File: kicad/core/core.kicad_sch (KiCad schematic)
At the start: 100 parts, among them J1 X_HS0_n, J10 ADDR_A0, J11 ADDR_A1, J12 ADDR_A2, J13 DEC_EN, J14 FWD_EN_n, J15 REV_EN_n, J2 Y_HS0_n, J3 X_LS0_n, J4 Y_LS0_n, J5 INH_EN_n, J6 X_HS0r_n, J7 Y_HS0r_n, J8 X_LS0r_n, J9 Y_LS0r_n, Q1 IRLZ44N, Q2 FDS8958A, Q3 FDS8958A, Q4 FDS8958A, Q5 FDS8958A, Q6 FDS8958A, U1 TLV3501AID, U10 TC4426A, U11 74AHC138, U12 74AHC138, U13 74AHC138, U14 74AHC138, U15 74AHC125, U16 74AHC125, U2 74AHC74, U3 OPA192, U4 TL431LP, U5 TC4427A, U6 TC4426A, U7 TC4427A, U8 TC4426A, U9 TC4427A

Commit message: logical schematic blocks reorg
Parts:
- removed U15, U16: 74AHC125, Package_SO:SOIC-14_3.9x8.7mm_P1.27mm, symbol 74xx:74LS125
- added C25, C26: 100n, Capacitor_SMD:C_0805_2012Metric, symbol Device:C
- added U15, U16, U17, U18: 74AHC138, Package_SO:SOIC-16_3.9x9.9mm_P1.27mm, symbol 74xx:74HC138
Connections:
- net DEC_XH0 is gone; now on net X_HS0_n: U11.15 (~{Y0})
- net DEC_XL0 is gone; now on net X_LS0_n: U12.15 (~{Y0})
- net DEC_YH0 is gone; now on net Y_HS0_n: U13.15 (~{Y0})
- net DEC_YL0 is gone; now on net Y_LS0_n: U14.15 (~{Y0})
- net +3V3: now also C25.1, C25.2, C26.1, C26.2, U15.16 (VCC), U15.5 (~{E1}), U15.8 (GND), U16.16 (VCC), U16.5 (~{E1}), U16.8 (GND), U17.16 (VCC), U17.5 (~{E1}), U17.8 (GND), U18.16 (VCC), U18.5 (~{E1}), U18.8 (GND); no longer J13.1 (Pin_1), R22.1, U11.4 (~{E0}), U11.6 (E2), U12.4 (~{E0}), U12.6 (E2), U13.4 (~{E0}), U13.6 (E2), U14.4 (~{E0}), U14.6 (E2)
- net ADDR_A0: now also U15.1 (A0), U16.1 (A0), U17.1 (A0), U18.1 (A0)
- net ADDR_A1: now also U15.2 (A1), U16.2 (A1), U17.2 (A1), U18.2 (A1)
- net ADDR_A2: now also U15.3 (A2), U16.3 (A2), U17.3 (A2), U18.3 (A2)
- net FWD_EN_n: now also U11.4 (~{E0}), U12.4 (~{E0}), U13.4 (~{E0}), U14.4 (~{E0})
- net REV_EN_n: now also U15.4 (~{E0}), U16.4 (~{E0}), U17.4 (~{E0}), U18.4 (~{E0})
- net X_HS0r_n: now also U15.15 (~{Y0})
- net X_LS0r_n: now also U16.15 (~{Y0})
- net Y_HS0r_n: now also U17.15 (~{Y0})
- net Y_LS0r_n: now also U18.15 (~{Y0})
- new net DEC_EN: J13.1 (Pin_1), R22.1, U11.6 (E2), U12.6 (E2), U13.6 (E2), U14.6 (E2), U15.6 (E2), U16.6 (E2), U17.6 (E2), U18.6 (E2)
- no-connect marks 52 -> 80
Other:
- note added: "CCS — Ic/2 sink"
- note added: "DECODE — FWD/REV 138 banks (1×1 / Y0)"
- note added: "DECODE: 74AHC138×4 FWD + ×4 REV; ~E0←FWD/REV_EN_n, ~E1←GND, E2←DEC_EN; ~Y0→*_n/*r_n; never assert both EN"
- note added: "DRIVE FWD — X0/Y0 matrix + gate"
- note added: "DRIVE REV — X0/Y0 matrix + gate"
- note added: "INHIBIT — series YB65→fold→YB66→CCS"
- note added: "QX/QY FDS8958A + SS14 → XA0/XB0 & YA0/YB0; LS → CCS_RET; TC442x below"
- note added: "QX0r/QY0r FDS8958A + SS14 swapped ends (HS→XB0/YB0, LS←XA0/YA0); LS→CCS_RET; TC442x below"
- note added: "SENSE — Bowtie / latch"
- note added: "SENSE — Bowtie / split-sense + amp Clamps: BAT54S rot90 — +3V3 (K) above, GND (A) below C1/C2 at U1; C3/C4 at U2; blocks spaced for hand placement"
- note added: "TL431 2.5V + pot divider → VSET; OPA192 drives IRLZ44N via R8; R9=1Ω; CCS_RET → Drive FWD/REV + Inhibit"
- note removed: "74AHC138×4 → DEC_*0; 74AHC125×2 steer FWD_EN_n→*_n / REV_EN_n→*r_n; ADDR default 000; never assert both EN"
- note removed: "QX/QY FDS8958A + SS14 → XA0/XB0 & YA0/YB0; LS → CCS_RET; gates labeled for Stage 4"
- note removed: "QX0r/QY0r FDS8958A + SS14 swapped ends (HS→XB0/YB0, LS←XA0/YA0); LS→CCS_RET; gates for Stage 7"
- note removed: "STAGE 1 — Sense / Bowtie"
- note removed: "STAGE 2 — CCS (Ic/2 sink)"
- note removed: "STAGE 3 — X/Y forward drive"
- note removed: "STAGE 4 — Gate drive (fail-safe pull-ups)"
- note removed: "STAGE 5 — Inhibit (series YB65→bowtie→YB66→CCS)"
- note removed: "STAGE 6 — X/Y reverse WRITE drive"
- note removed: "STAGE 7 — Reverse gate drive (fail-safe pull-ups)"
- note removed: "STAGE 8 — Address decode (1×1 / Y0 only)"
- note removed: "Stage 1 — Bowtie / split-sense + amp Clamps: BAT54S rot90 — +3V3 (K) above, GND (A) below C1/C2 at U1; C3/C4 at U2; blocks spaced for hand placement"
- note removed: "TL431 2.5V + pot divider → VSET; OPA192 drives IRLZ44N via R8; R9=1Ω; CCS_RET → Stage 3/5"
- title: Core Memory Driver — Stage 1 Sense / Bowtie -> Core Memory Driver

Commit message: Split the schematic into hierarchical blocks and document the net grammar.
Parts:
- removed C1, C11, C13, C15, C17, C19, C20, C21, C22, C23, C24, C25, C26, C3, C5, C7, C9: 100n, Capacitor_SMD:C_0805_2012Metric, symbol Device:C
- removed C10, C12, C14, C16, C18, C2, C4, C6, C8: 1u, Capacitor_SMD:C_0805_2012Metric, symbol Device:C
- removed D1, D2: BAT54S, Package_TO_SOT_SMD:SOT-23, symbol Diode:BAT54S
- removed D10, D3, D4, D5, D6, D7, D8, D9: SS14, Diode_SMD:D_SMA, symbol Diode:SS14
- removed FB1: FB_A, Inductor_SMD:L_1206_3216Metric, symbol core_memory:CoreBead_3W
- removed FB2: FB_B, Inductor_SMD:L_1206_3216Metric, symbol core_memory:CoreBead_3W
- removed J1: X_HS0_n, Connector_PinHeader_2.54mm:PinHeader_1x01_P2.54mm_Vertical, symbol Connector:Conn_01x01
- removed J10: ADDR_A0, Connector_PinHeader_2.54mm:PinHeader_1x01_P2.54mm_Vertical, symbol Connector:Conn_01x01
- removed J11: ADDR_A1, Connector_PinHeader_2.54mm:PinHeader_1x01_P2.54mm_Vertical, symbol Connector:Conn_01x01
- removed J12: ADDR_A2, Connector_PinHeader_2.54mm:PinHeader_1x01_P2.54mm_Vertical, symbol Connector:Conn_01x01
- removed J13: DEC_EN, Connector_PinHeader_2.54mm:PinHeader_1x01_P2.54mm_Vertical, symbol Connector:Conn_01x01
- removed J14: FWD_EN_n, Connector_PinHeader_2.54mm:PinHeader_1x01_P2.54mm_Vertical, symbol Connector:Conn_01x01
- removed J15: REV_EN_n, Connector_PinHeader_2.54mm:PinHeader_1x01_P2.54mm_Vertical, symbol Connector:Conn_01x01
- removed J2: Y_HS0_n, Connector_PinHeader_2.54mm:PinHeader_1x01_P2.54mm_Vertical, symbol Connector:Conn_01x01
- removed J3: X_LS0_n, Connector_PinHeader_2.54mm:PinHeader_1x01_P2.54mm_Vertical, symbol Connector:Conn_01x01
- removed J4: Y_LS0_n, Connector_PinHeader_2.54mm:PinHeader_1x01_P2.54mm_Vertical, symbol Connector:Conn_01x01
- removed J5: INH_EN_n, Connector_PinHeader_2.54mm:PinHeader_1x01_P2.54mm_Vertical, symbol Connector:Conn_01x01
- removed J6: X_HS0r_n, Connector_PinHeader_2.54mm:PinHeader_1x01_P2.54mm_Vertical, symbol Connector:Conn_01x01
- removed J7: Y_HS0r_n, Connector_PinHeader_2.54mm:PinHeader_1x01_P2.54mm_Vertical, symbol Connector:Conn_01x01
- removed J8: X_LS0r_n, Connector_PinHeader_2.54mm:PinHeader_1x01_P2.54mm_Vertical, symbol Connector:Conn_01x01
- removed J9: Y_LS0r_n, Connector_PinHeader_2.54mm:PinHeader_1x01_P2.54mm_Vertical, symbol Connector:Conn_01x01
- removed Q1: IRLZ44N, Package_TO_SOT_THT:TO-220-3_Vertical, symbol Transistor_FET:IRLZ44N
- removed Q2, Q3, Q4, Q5, Q6: FDS8958A, Package_SO:SOIC-8_3.9x4.9mm_P1.27mm, symbol core_memory:FDS8958A
- removed R1, R10, R11, R12, R13, R14, R15, R16, R17, R18, R19, R20, R21, R22, R23, R24, R6: 10k, Resistor_SMD:R_0805_2012Metric, symbol Device:R
- removed R2, R5: DNP, Resistor_SMD:R_0805_2012Metric, symbol Device:R
- removed R3, R4, R7: 1k, Resistor_SMD:R_0805_2012Metric, symbol Device:R
- removed R8: 100, Resistor_SMD:R_0805_2012Metric, symbol Device:R
- removed R9: 1, Resistor_SMD:R_2512_6332Metric, symbol Device:R
- removed RV1: 10k, Potentiometer_THT:Potentiometer_Bourns_3296W_Vertical, symbol Device:R_Potentiometer_US
- removed TP1: DOUT, TestPoint:TestPoint_Pad_D1.5mm, symbol Connector:TestPoint
- removed TP2: Isense, TestPoint:TestPoint_Pad_D1.5mm, symbol Connector:TestPoint
- removed U1: TLV3501AID, Package_SO:SOIC-8_3.9x4.9mm_P1.27mm, symbol Comparator:TLV3501AID
- removed U10, U6, U8: TC4426A, Package_SO:SOIC-8_3.9x4.9mm_P1.27mm, symbol Driver_FET:TC4426xOA
- removed U11, U12, U13, U14, U15, U16, U17, U18: 74AHC138, Package_SO:SOIC-16_3.9x9.9mm_P1.27mm, symbol 74xx:74HC138
- removed U2: 74AHC74, Package_SO:SOIC-14_3.9x8.7mm_P1.27mm, symbol 74xx:74LS74
- removed U3: OPA192, Package_SO:SOIC-8_3.9x4.9mm_P1.27mm, symbol core_memory:OPA192
- removed U4: TL431LP, Package_TO_SOT_THT:TO-92_Inline, symbol Reference_Voltage:TL431LP
- removed U5, U7, U9: TC4427A, Package_SO:SOIC-8_3.9x4.9mm_P1.27mm, symbol Driver_FET:TC4427xOA
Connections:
- no-connect marks 80 -> 8
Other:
- added sheet CCS (ccs.kicad_sch)
- added sheet Decode Block (decode_block.kicad_sch)
- added sheet Decode CTRL (decode_ctrl.kicad_sch)
- added sheet Decoupling Logic (decoupling_logic.kicad_sch)
- added sheet Decoupling VDRIVE (decoupling_vdrive.kicad_sch)
- added sheet Drive Block (drive_block.kicad_sch)
- added sheet Ferrite Beads (ferrite_beads.kicad_sch)
- added sheet Inhibit (inhibit.kicad_sch)
- added sheet Sense (sense.kicad_sch)
- note added: "DECODE — Decode Block (N=axis, n=HS/LS bank); X FWD wired for 1×1 bring-up"
- note added: "DRIVE — Drive Block (N=axis, n=line); X0 FWD wired for 1×1 bring-up"
- note added: "Decoupling (global power) — caps off the signal pages"
- note added: "SENSE / FERRITE BEADS / CCS / INHIBIT / DECODE CTRL — hierarchy"
- note removed: "CCS — Ic/2 sink"
- note removed: "DECODE — FWD/REV 138 banks (1×1 / Y0)"
- note removed: "DECODE: 74AHC138×4 FWD + ×4 REV; ~E0←FWD/REV_EN_n, ~E1←GND, E2←DEC_EN; ~Y0→*_n/*r_n; never assert both EN"
- note removed: "DRIVE FWD — X0/Y0 matrix + gate"
- note removed: "DRIVE REV — X0/Y0 matrix + gate"
- note removed: "INHIBIT — series YB65→fold→YB66→CCS"
- note removed: "QX/QY FDS8958A + SS14 → XA0/XB0 & YA0/YB0; LS → CCS_RET; TC442x below"
- note removed: "QX0r/QY0r FDS8958A + SS14 swapped ends (HS→XB0/YB0, LS←XA0/YA0); LS→CCS_RET; TC442x below"
- note removed: "SENSE — Bowtie / latch"
- note removed: "SENSE — Bowtie / split-sense + amp Clamps: BAT54S rot90 — +3V3 (K) above, GND (A) below C1/C2 at U1; C3/C4 at U2; blocks spaced for hand placement"
- note removed: "TC4427A → X/Y_HS0; TC4426A → X/Y_LS0; 10k to +3V3 on *_n; VDRIVE power; headers J1–J4"
- note removed: "TC4427A → X/Y_HS0r; TC4426A → X/Y_LS0r; 10k to +3V3 on *r_n; headers J6–J9"
- note removed: "TL431 2.5V + pot divider → VSET; OPA192 drives IRLZ44N via R8; R9=1Ω; CCS_RET → Drive FWD/REV + Inhibit"

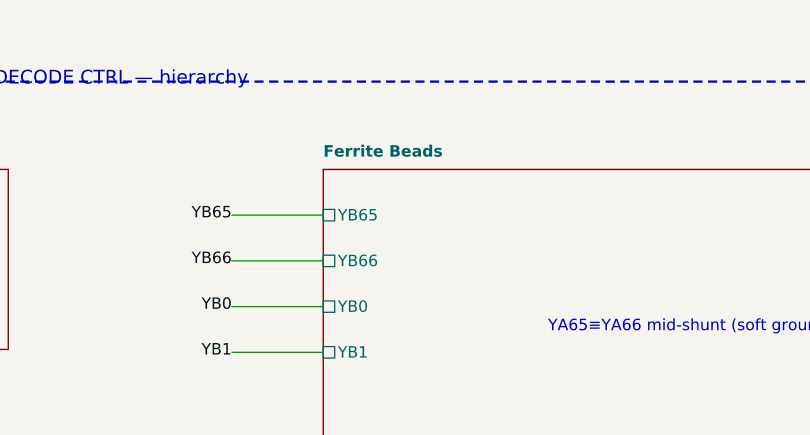
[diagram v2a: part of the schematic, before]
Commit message: created new component based on simulation and replace resistive model with inductive model
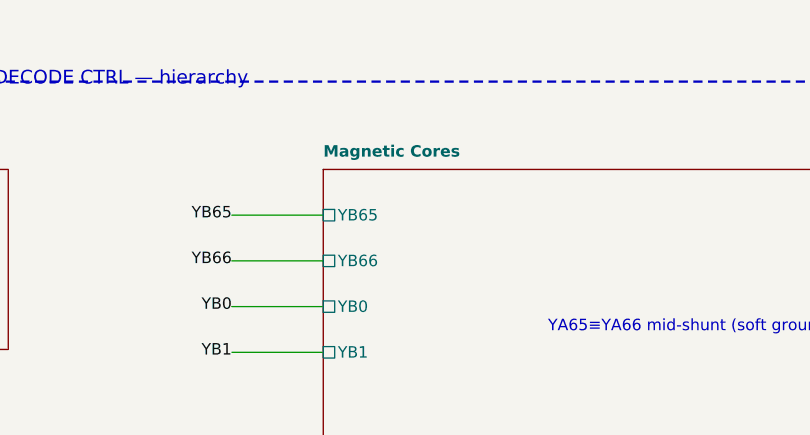
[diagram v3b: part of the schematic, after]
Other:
- sheet Ferrite Beads renamed Magnetic Cores
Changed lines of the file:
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@@
 			(color 0 0 0 0)
 		)
-		(property "Sheetname" "Ferrite Beads"
+		(property "Sheetname" "Magnetic Cores"
 			(at 100 23.73 0)
 			(show_name no)

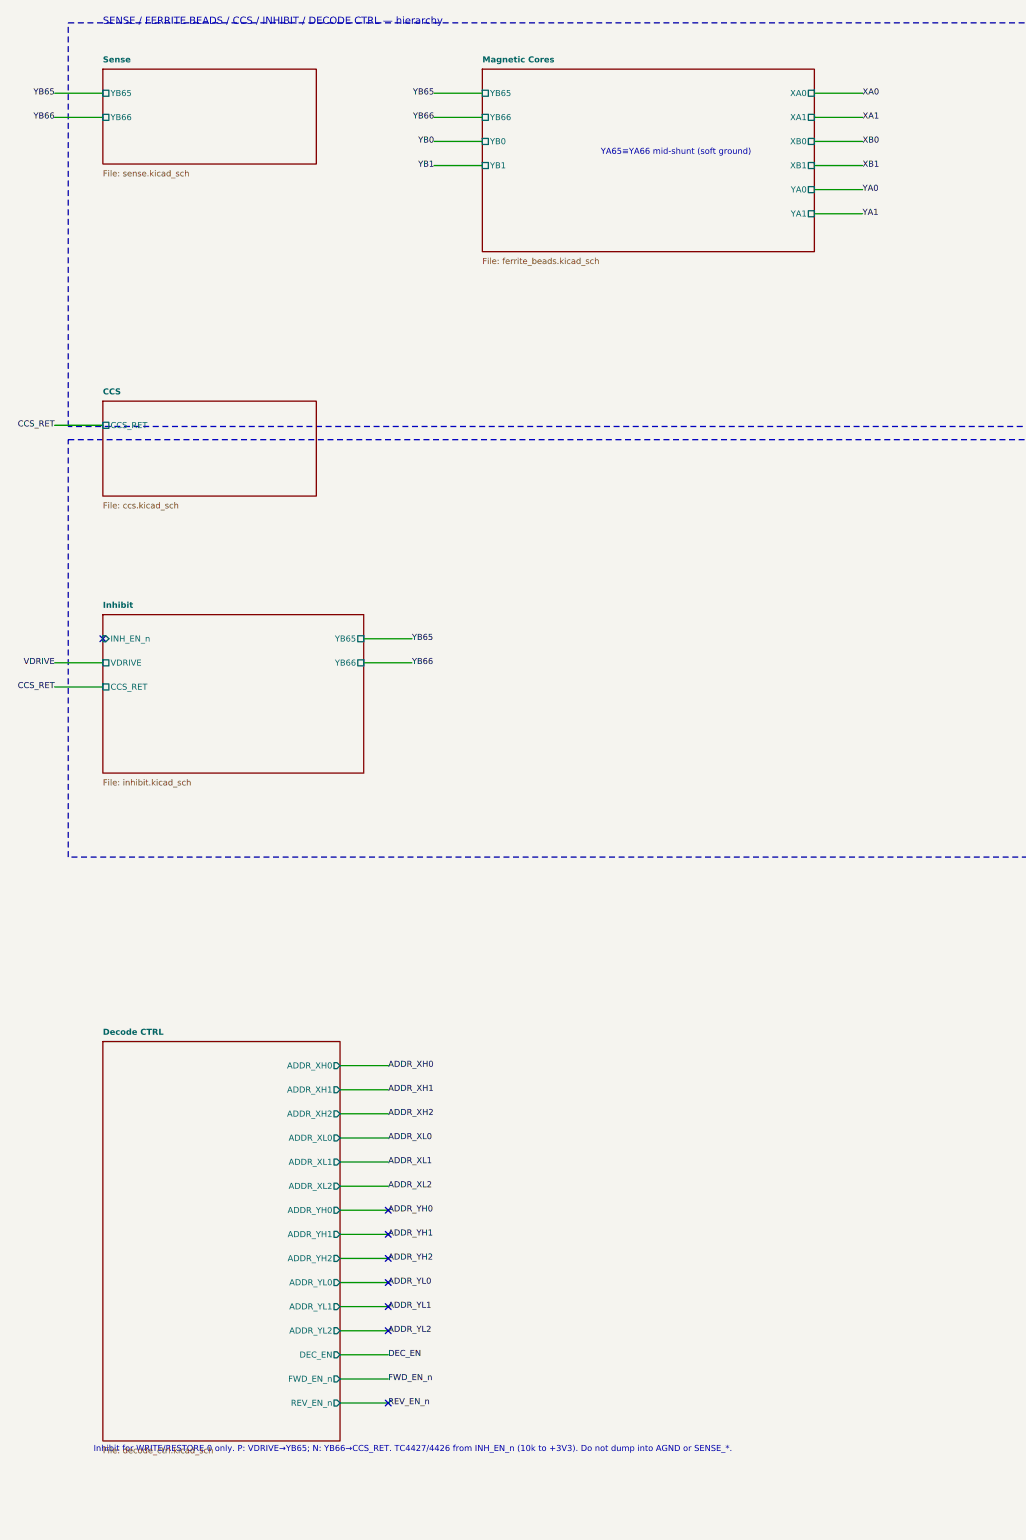
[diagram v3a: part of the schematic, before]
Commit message: Docs updated to match physical core layout.
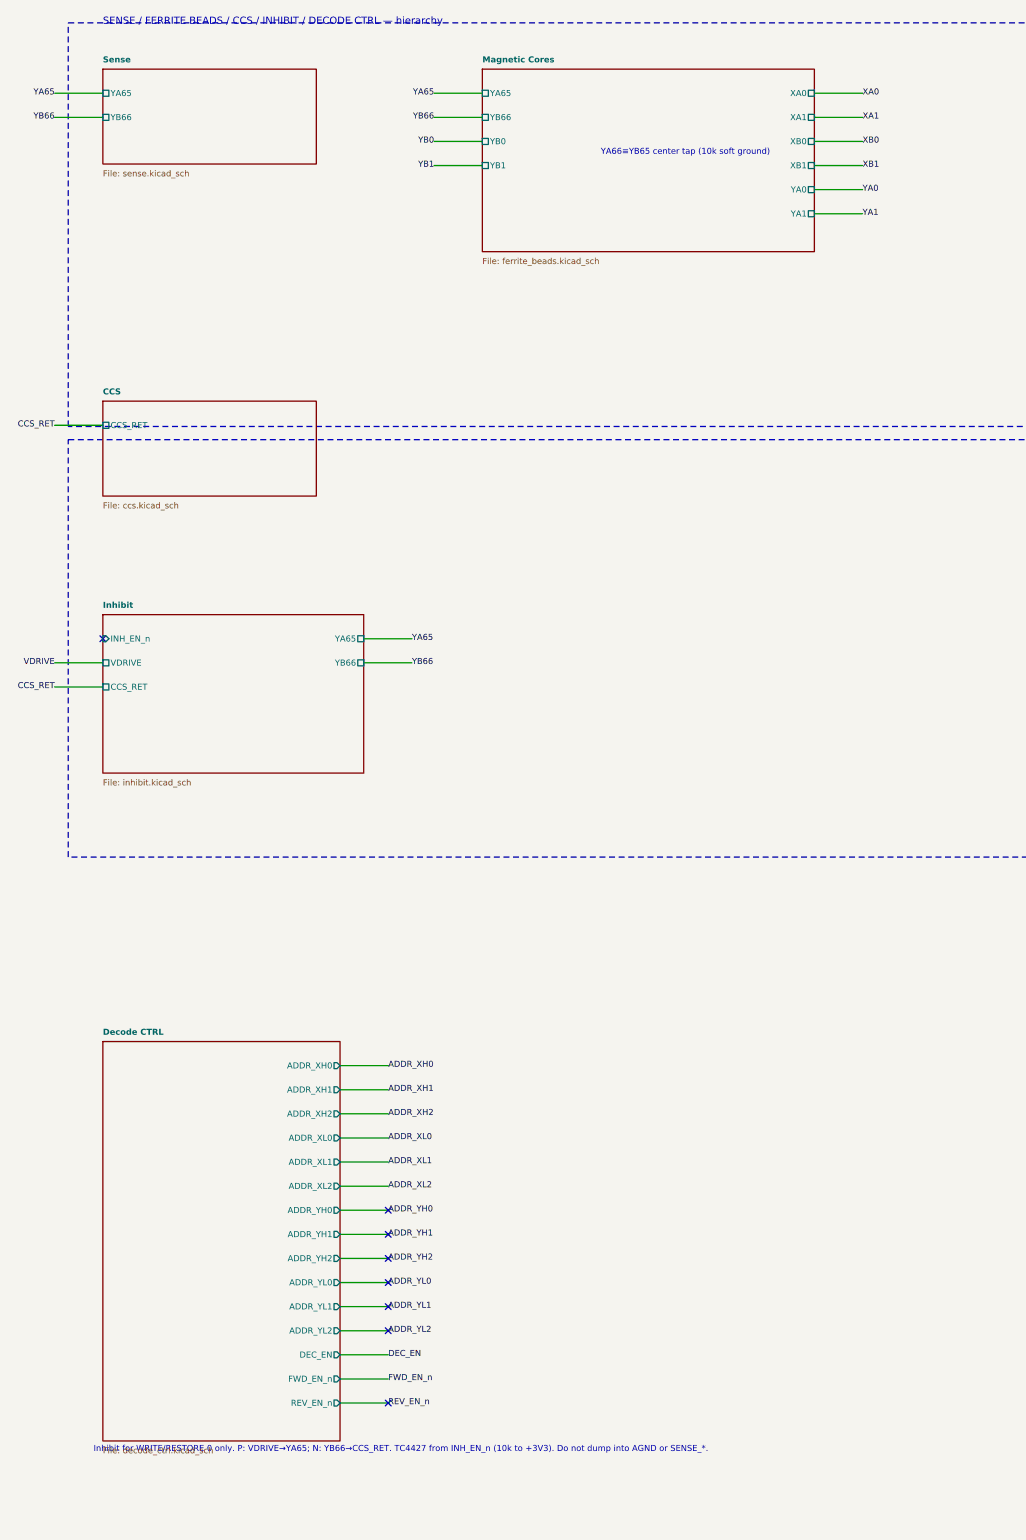
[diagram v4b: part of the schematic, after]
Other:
- sheet Inhibit ports: added YA65; removed YB65
- sheet Magnetic Cores ports: added YA65; removed YB65
- sheet Sense ports: added YA65; removed YB65
- note added: "Inhibit for WRITE/RESTORE 0 only. P: VDRIVE→YA65; N: YB66→CCS_RET. TC4427 from INH_EN_n (10k to +3V3). Do not dump into AGND or SENSE_*."
- note added: "YA66≡YB65 center tap (10k soft ground)"
- note removed: "Inhibit for WRITE/RESTORE 0 only. P: VDRIVE→YB65; N: YB66→CCS_RET. TC4427/4426 from INH_EN_n (10k to +3V3). Do not dump into AGND or SENSE_*."
- note removed: "YA65≡YA66 mid-shunt (soft ground)"
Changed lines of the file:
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@@
 	(title_block
 		(title "Core Memory Driver")
-		(comment 1 "Bowtie FB_A/FB_B; soft YA mid; iso + clamps; TLV3501; 74AHC74")
+		(comment 1 "2x2 MCE; YA66=YB65 center tap; YA65/YB66 sense and inhibit; TLV3501; 74AHC74")
 	)
 	(rectangle
@@
 		)
 	)
-	(text "YA65≡YA66 mid-shunt (soft ground)"
+	(text "YA66≡YB65 center tap (10k soft ground)"
 		(exclude_from_sim no)
 		(at 124.968 42.522 0)
@@
 		)
 	)
-	(text "Inhibit for WRITE/RESTORE 0 only. P: VDRIVE→YB65; N: YB66→CCS_RET. TC4427/4426 from INH_EN_n (10k to +3V3). Do not dump into AGND or SENSE_*."
+	(text "Inhibit for WRITE/RESTORE 0 only. P: VDRIVE→YA65; N: YB66→CCS_RET. TC4427 from INH_EN_n (10k to +3V3). Do not dump into AGND or SENSE_*."
 		(exclude_from_sim no)
 		(at 18.034 315.976 0)
@@
 		)
 	)
-	(label "YB65"
+	(label "YA65"
 		(at 85.16 145.08 0)
 		(effects
@@
 		)
 	)
-	(label "YB65"
+	(label "YA65"
 		(at 9.84 30.08 180)
 		(effects
@@
 		)
 	)
-	(label "YB65"
+	(label "YA65"
 		(at 89.84 30.08 180)
 		(effects
@@
 			)
 		)
-		(pin "YB65" passive
+		(pin "YA65" passive
 			(at 20 30.08 180)
 			(effects
@@
 			)
 		)
-		(pin "YB65" passive
+		(pin "YA65" passive
 			(at 75 145.08 0)
 			(effects
@@
 			)
 		)
-		(pin "YB65" passive
+		(pin "YA65" passive
 			(at 100 30.08 180)
 			(effects
